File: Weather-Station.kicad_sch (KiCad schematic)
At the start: 3 parts, among them J1 Conn_01x22, J2 Conn_01x22, U1 ESP32-S3-DevKitC

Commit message: WIP: Finding pin headers/rows
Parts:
- added J3, J4: Conn_02x19_Odd_Even, Connector_PinHeader_2.54mm:PinHeader_2x19_P2.54mm_Vertical, symbol Connector_Generic:Conn_02x19_Odd_Even
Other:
- moved on the sheet: J1, J2, U1

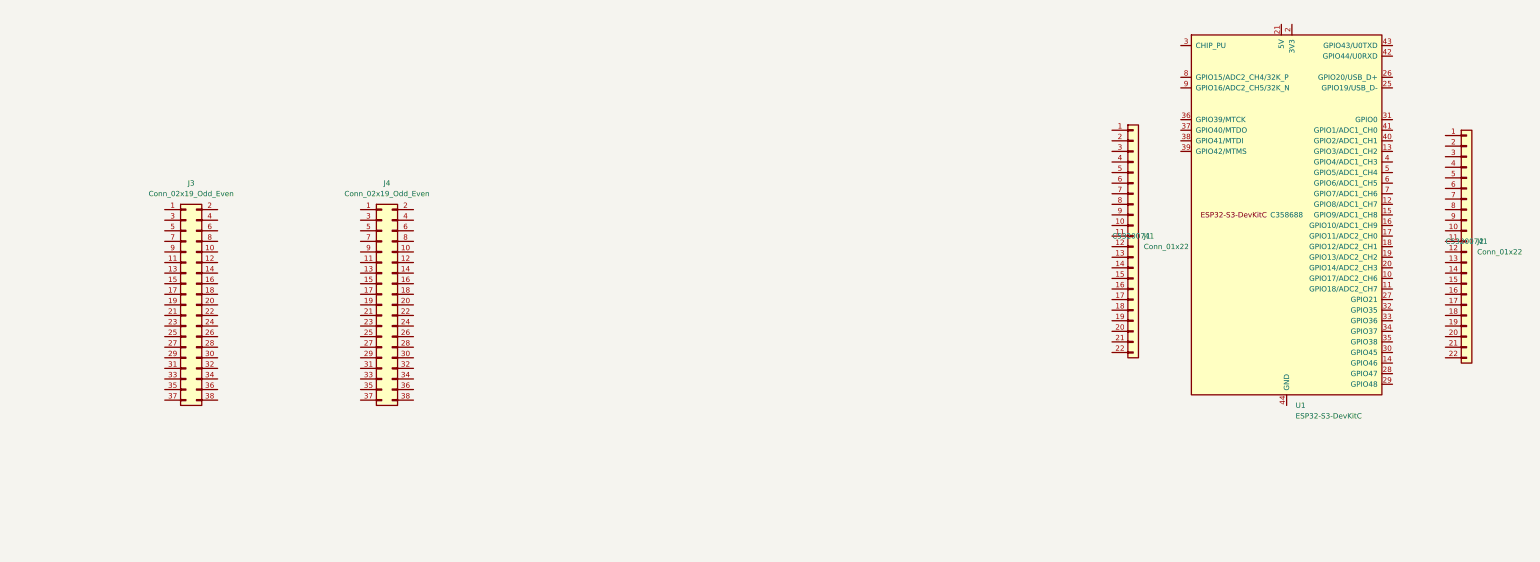
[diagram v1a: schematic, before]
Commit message: WIP: Adding display and ESP32
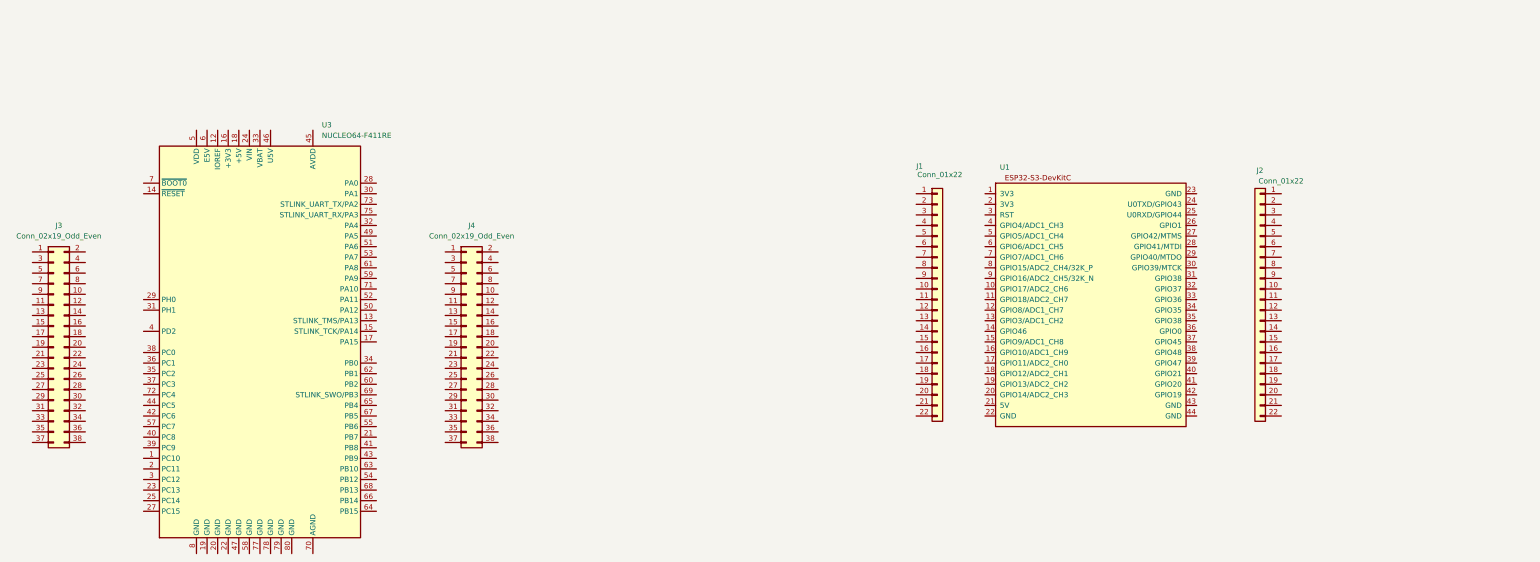
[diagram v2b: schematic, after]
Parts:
- added U3: NUCLEO64-F411RE, custom:ST_NUCLEO-GFX01M2, symbol MCU_Module:NUCLEO64-F411RE
- U1: LCSC C358688 -> (none); now left out of the parts list
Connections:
- net at U1.1 (3V3): no longer U1.2 (3V3)
- now unconnected: U1.22 (GND), U1.23 (GND), U1.24 (GND), U1.44 (GND)
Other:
- moved on the sheet: J1, J2, J3, J4

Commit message: WIP: Finding components on jlcpcb and merging
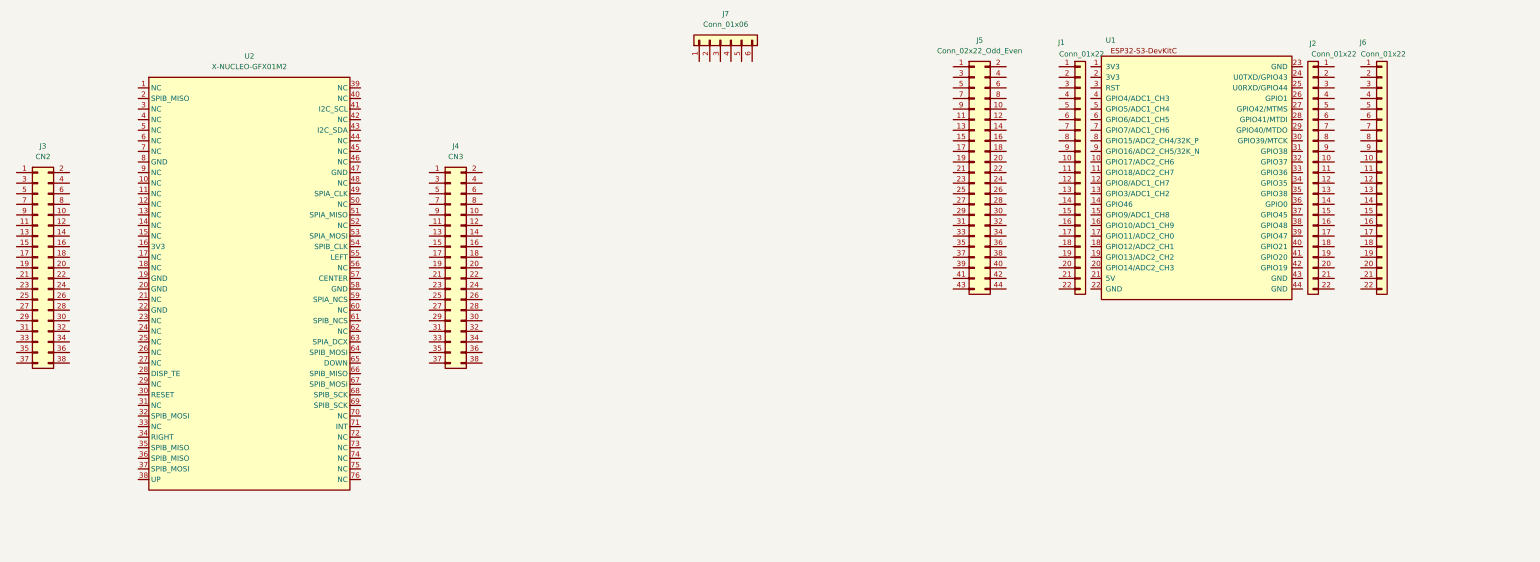
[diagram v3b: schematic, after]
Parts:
- removed U3: NUCLEO64-F411RE, custom:ST_NUCLEO-GFX01M2, symbol MCU_Module:NUCLEO64-F411RE
- added J5: Conn_02x22_Odd_Even, Connector_PinHeader_2.54mm:PinHeader_2x22_P2.54mm_Vertical, symbol Connector_Generic:Conn_02x22_Odd_Even
- added J6: Conn_01x22, Connector_PinHeader_2.54mm:PinHeader_1x22_P2.54mm_Vertical, symbol Connector_Generic:Conn_01x22
- added J7: Conn_01x06, Connector_PinSocket_2.54mm:PinSocket_1x06_P2.54mm_Vertical, symbol Connector_Generic:Conn_01x06
- added U2: X-NUCLEO-GFX01M2, custom:ST_NUCLEO-GFX01M2, symbol New_Library_1:X-NUCLEO_GFX01M2
- J3: value Conn_02x19_Odd_Even -> CN2
- J4: value Conn_02x19_Odd_Even -> CN3
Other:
- moved on the sheet: J1, J2, J3, J4, U1

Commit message: WIP: Started routing
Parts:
- U1, U2: now not fitted
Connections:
- net at J6.1 (Pin_1): now also J2.1 (Pin_1)
- net at J6.10 (Pin_10): now also J2.10 (Pin_10)
- net at J6.11 (Pin_11): now also J2.11 (Pin_11)
- net at J6.12 (Pin_12): now also J2.12 (Pin_12)
- net at J6.13 (Pin_13): now also J2.13 (Pin_13)
- net at J6.14 (Pin_14): now also J2.14 (Pin_14)
- net at J6.15 (Pin_15): now also J2.15 (Pin_15)
- net at J6.16 (Pin_16): now also J2.16 (Pin_16)
- net at J6.17 (Pin_17): now also J2.17 (Pin_17)
- net at J6.18 (Pin_18): now also J2.18 (Pin_18)
- net at J6.19 (Pin_19): now also J2.19 (Pin_19)
- net at J6.2 (Pin_2): now also J2.2 (Pin_2)
- net at J6.20 (Pin_20): now also J2.20 (Pin_20)
- net at J6.21 (Pin_21): now also J2.21 (Pin_21)
- net at J6.22 (Pin_22): now also J2.22 (Pin_22)
- net at J6.3 (Pin_3): now also J2.3 (Pin_3)
- net at J6.4 (Pin_4): now also J2.4 (Pin_4)
- net at J6.5 (Pin_5): now also J2.5 (Pin_5)
- net at J6.6 (Pin_6): now also J2.6 (Pin_6)
- net at J6.7 (Pin_7): now also J2.7 (Pin_7)
- net at J6.8 (Pin_8): now also J2.8 (Pin_8)
- net at J6.9 (Pin_9): now also J2.9 (Pin_9)
- net at J5.1 (Pin_1): now also J3.16 (Pin_16)
- net at J5.10 (Pin_10): now also J1.5 (Pin_5)
- net at J5.12 (Pin_12): now also J1.6 (Pin_6)
- net at J5.14 (Pin_14): now also J1.7 (Pin_7)
- net at J5.16 (Pin_16): now also J1.8 (Pin_8)
- net at J5.18 (Pin_18): now also J1.9 (Pin_9)
- net at J5.2 (Pin_2): now also J1.1 (Pin_1)
- net at J5.20 (Pin_20): now also J1.10 (Pin_10)
- net at J5.22 (Pin_22): now also J1.11 (Pin_11)
- net at J5.24 (Pin_24): now also J1.12 (Pin_12)
- net at J5.26 (Pin_26): now also J1.13 (Pin_13)
- net at J5.28 (Pin_28): now also J1.14 (Pin_14)
- net at J5.30 (Pin_30): now also J1.15 (Pin_15)
- net at J5.32 (Pin_32): now also J1.16 (Pin_16)
- net at J5.34 (Pin_34): now also J1.17 (Pin_17)
- net at J5.36 (Pin_36): now also J1.18 (Pin_18)
- net at J5.38 (Pin_38): now also J1.19 (Pin_19)
- net at J5.4 (Pin_4): now also J1.2 (Pin_2)
- net at J5.40 (Pin_40): now also J1.20 (Pin_20)
- net at J5.42 (Pin_42): now also J1.21 (Pin_21)
- net at J5.44 (Pin_44): now also J1.22 (Pin_22)
- net at J5.6 (Pin_6): now also J1.3 (Pin_3)
- net at J5.8 (Pin_8): now also J1.4 (Pin_4)
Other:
- title: (none) -> Weather Station PCB
- moved on the sheet: J1, J2, J3, J4, J5, J6

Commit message: WIP: Routing started
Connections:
- net GND: now reaches J2.1 (Pin_1), J6.1 (Pin_1)
- net GND: now also J2.21 (Pin_21), J2.22 (Pin_22), J5.43 (Pin_43), J6.21 (Pin_21), J6.22 (Pin_22), J7.2 (Pin_2), J7.5 (Pin_5)
- net +3.3V: now reaches J7.1 (Pin_1)
- net +3.3V: now also J5.1 (Pin_1), J5.3 (Pin_3), J7.6 (Pin_6)
- net BME_SDA: now reaches J7.3 (Pin_3)
- net BME_SDA: now also J5.23 (Pin_23)
- net BME_SCL: now reaches J7.4 (Pin_4)
- net BME_SCL: now also J5.29 (Pin_29)
- net at J3.16 (Pin_16): no longer J5.1 (Pin_1)
- net CENTER: now reaches J5.13 (Pin_13)
- net CENTER: now also J4.19 (Pin_19)
- net RIGHT: now reaches J5.15 (Pin_15)
- net RIGHT: now also J3.34 (Pin_34)
- net DOWN: now reaches J5.17 (Pin_17)
- net DOWN: now also J4.27 (Pin_27)
- net LEFT: now reaches J5.19 (Pin_19)
- net LEFT: now also J4.17 (Pin_17)
- net UP: now reaches J5.21 (Pin_21)
- net UP: now also J3.38 (Pin_38)
- net DISP_DC: now reaches J5.27 (Pin_27)
- net DISP_DC: now also J4.25 (Pin_25)
- net DISP_CS: now reaches J5.31 (Pin_31)
- net DISP_CS: now also J4.21 (Pin_21)
- net DISP_MOSI: now reaches J5.33 (Pin_33)
- net DISP_MOSI: now also J4.15 (Pin_15)
- net DISP_SCLK: now reaches J5.35 (Pin_35)
- net DISP_SCLK: now also J4.11 (Pin_11)
- net DISP_RESET: now reaches J5.39 (Pin_39)
- net DISP_RESET: now also J3.30 (Pin_30)
- net +5V: now reaches J5.41 (Pin_41)
- no-connect marks 0 -> 127

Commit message: Routing done
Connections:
- net +3.3V: now also J3.16 (Pin_16)
- net GND: now also J1.22 (Pin_22), J3.19 (Pin_19), J3.20 (Pin_20), J3.22 (Pin_22), J3.8 (Pin_8), J4.20 (Pin_20), J4.9 (Pin_9), J5.44 (Pin_44)
- no-connect marks 127 -> 187
